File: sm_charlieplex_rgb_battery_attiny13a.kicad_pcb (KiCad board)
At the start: 2 copper layers, 12 x 12 mm, 12 parts, among them SW1 SW_Push, U1 ATtiny10-TS

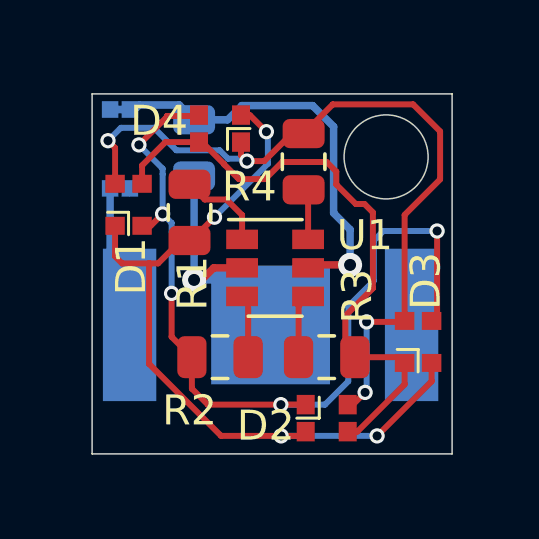
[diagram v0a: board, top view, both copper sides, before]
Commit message: Reformat for attiny13
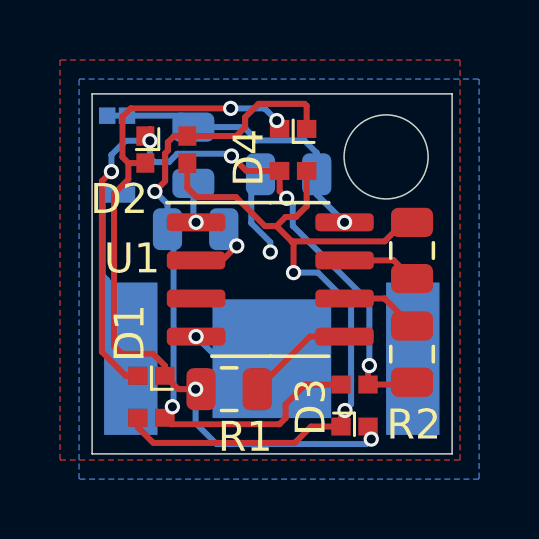
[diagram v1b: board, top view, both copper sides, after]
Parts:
- added R5: 10kR, Resistor_SMD:R_0805_2012Metric, B.Cu at (168.3, 106.0)
- R4: moved to B.Cu
- U1: value ATtiny10-TS -> ATtiny13A-SSU; footprint Package_TO_SOT_SMD:SOT-23-6 -> Package_SO:SOIC-8_3.9x4.9mm_P1.27mm
- moved D2 10.4 mm to (167.4, 105.9)
- moved D1 6.45 mm to (166.9, 114.1), turned to 90 degrees
- moved R2 6.40 mm to (175.6, 112.7), turned to 90 degrees
- moved R1 6.04 mm to (169.5, 113.8), turned to 0 degrees
- moved R3 4.55 mm to (175.6, 109.2), turned to 270 degrees
- moved R4 4.24 mm to (168.4, 108.5), turned to 0 degrees
- moved C1 3.27 mm to (171.4, 106.7), turned to 180 degrees
- moved D3 3.00 mm to (173.6, 114.4)
- moved D4 2.54 mm to (171.6, 105.9), turned to 90 degrees
- moved BT1 1.13 mm to (170.9, 112.8)
- moved U1 0.42 mm to (170.8, 110.2)
- moved SW1 0.23 mm to (165.7, 106.0)
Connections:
- U1 pad 1: Net-(R1-Pad2) -> Net-(R5-Pad1)
- U1 pad 2: /GND -> Net-(R4-Pad2)
- U1 pad 3: Net-(R2-Pad2) -> Net-(U1-Pad3)
- U1 pad 4: Net-(R3-Pad2) -> /GND
- U1 pad 5: Net-(C1-Pad1) -> Net-(R1-Pad2)
- U1 pad 6: Net-(R4-Pad2) -> Net-(R2-Pad2)
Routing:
- net Net-(D1-Pad2): track 20.7 -> 26.9 mm, vias 0 -> 2
- net Net-(C1-Pad1): track 15.4 -> 10.2 mm
- net Net-(D1-Pad3): track 29.1 -> 25.4 mm
- net Net-(D1-Pad1): track 26.3 -> 23.0 mm, vias 4 -> 2
- net /GND: track 8.40 -> 5.81 mm, vias 1 -> 2
- net /+3V: track 8.76 -> 6.58 mm
- net Net-(R5-Pad1): track 0.00 -> 1.34 mm, vias 0 -> 1
- net Net-(R4-Pad2): track 1.71 -> 2.30 mm, vias 0 -> 1
- net Net-(R1-Pad2): track 3.07 -> 3.64 mm
- net Net-(R2-Pad2): track 2.11 -> 2.63 mm
- added copper zone on B.Cu, net /GND
- added copper zone on F.Cu, net /GND
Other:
- board text removed: "WM v2.0.0 09/25/19"
